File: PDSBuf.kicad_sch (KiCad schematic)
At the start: 23 parts

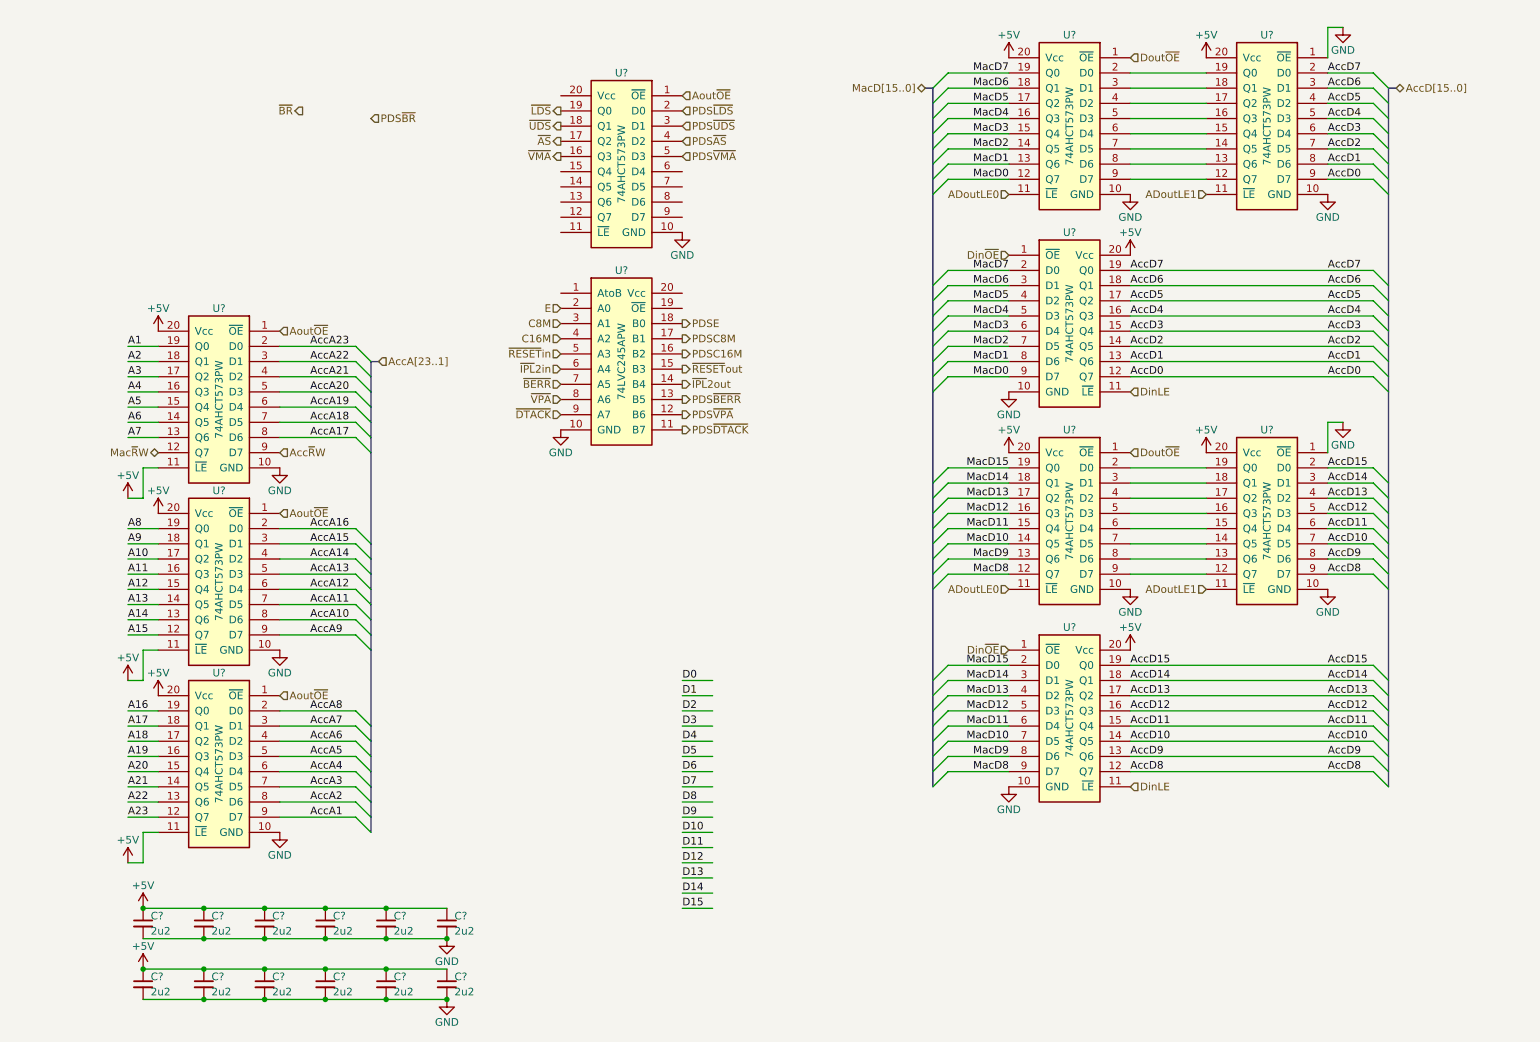
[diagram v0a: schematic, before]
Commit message: Switch to '030
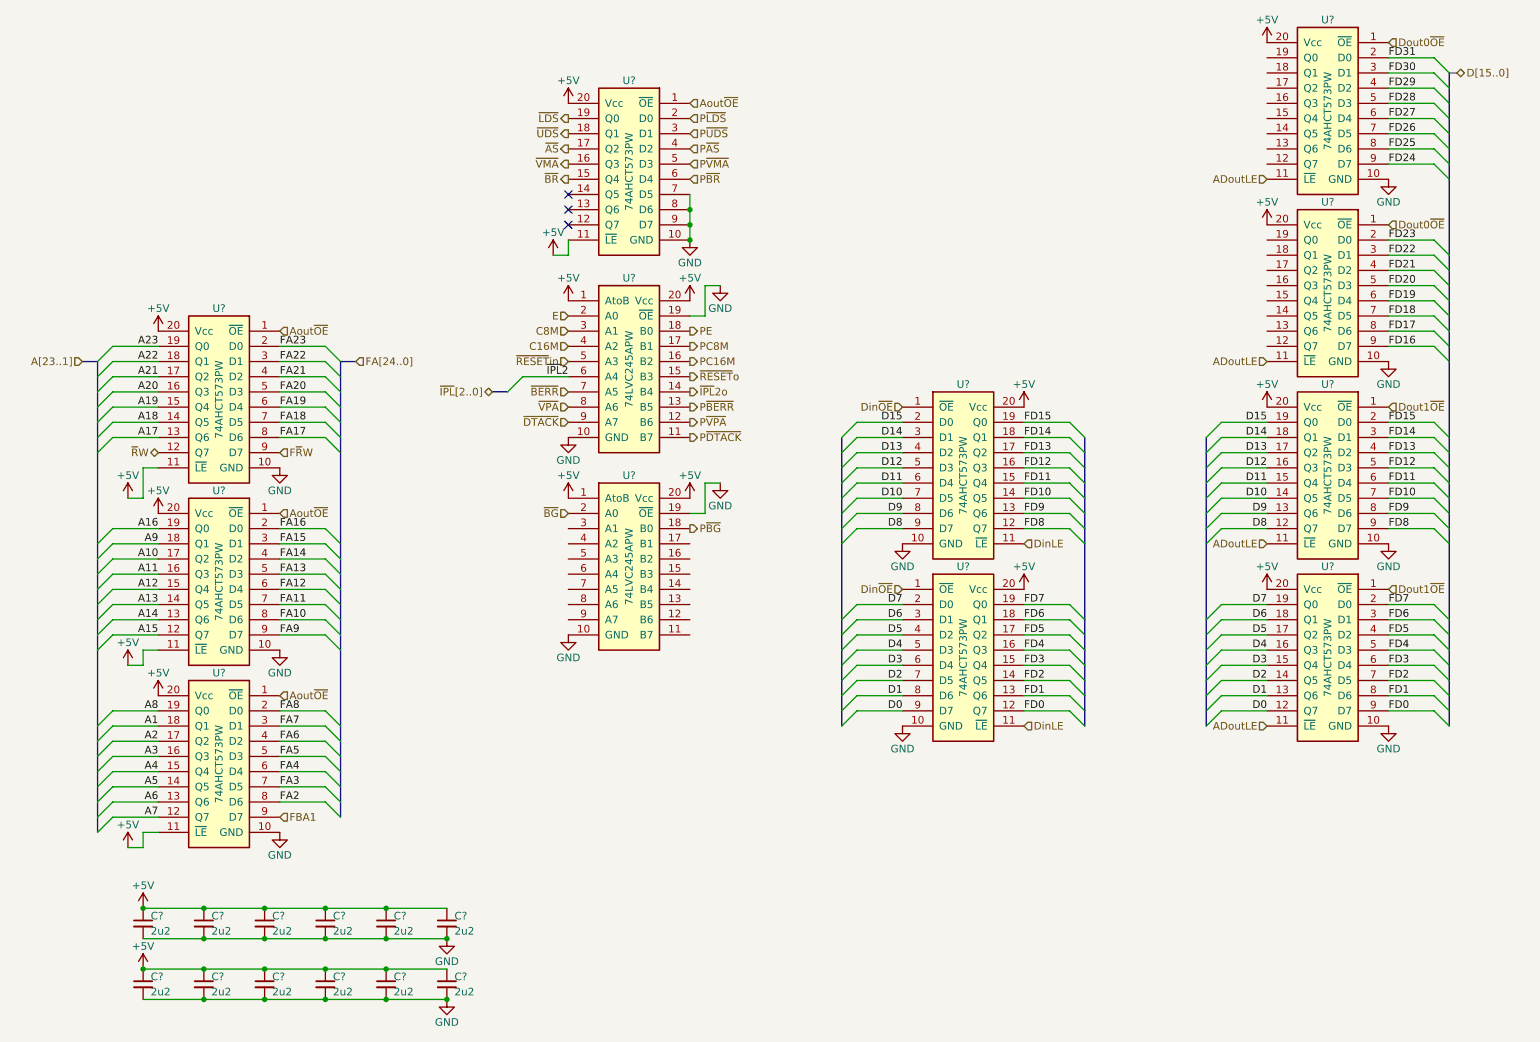
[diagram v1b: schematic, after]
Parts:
- removed U? (x5): 74AHCT573PW, stdpads:TSSOP-20_4.4x6.5mm_P0.65mm, symbol GW_Logic:74573
- added U? (x5): 74AHCT573PW, stdpads:TSSOP-20_4.4x6.5mm_P0.65mm, symbol GW_Logic:74573
- added U?: 74LVC245APW, symbol GW_Logic:74245
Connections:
- net +5V: now also U?.1 (AtoB), U?.11 (~{LE}), U?.20 (Vcc), U?.20 (Vcc), U?.1 (AtoB), U?.20 (Vcc), U?.20 (Vcc), U?.20 (Vcc), U?.20 (Vcc), U?.20 (Vcc), U?.20 (Vcc)
- net A1: now also U?.18 (Q1); no longer U?.19 (Q0)
- net A16: now also U?.19 (Q0); no longer U?.19 (Q0)
- net A17: now also U?.13 (Q6); no longer U?.18 (Q1)
- net A18: now also U?.14 (Q5); no longer U?.17 (Q2)
- net A19: now also U?.15 (Q4); no longer U?.16 (Q3)
- net A2: now also U?.17 (Q2); no longer U?.18 (Q1)
- net A20: now also U?.16 (Q3); no longer U?.15 (Q4)
- net A21: now also U?.17 (Q2); no longer U?.14 (Q5)
- net A22: now also U?.18 (Q1); no longer U?.13 (Q6)
- net A23: now also U?.19 (Q0); no longer U?.12 (Q7)
- net A3: now also U?.16 (Q3); no longer U?.17 (Q2)
- net A4: now also U?.15 (Q4); no longer U?.16 (Q3)
- net A5: now also U?.14 (Q5); no longer U?.15 (Q4)
- net A6: now also U?.13 (Q6); no longer U?.14 (Q5)
- net A7: now also U?.12 (Q7); no longer U?.13 (Q6)
- net A8: now also U?.19 (Q0); no longer U?.19 (Q0)
- net D0: now also U?.12 (Q7), U?.9 (D7)
- net D1: now also U?.13 (Q6), U?.8 (D6)
- net D10: now also U?.14 (Q5), U?.7 (D5)
- net D11: now also U?.15 (Q4), U?.6 (D4)
- net D12: now also U?.16 (Q3), U?.5 (D3)
- net D13: now also U?.17 (Q2), U?.4 (D2)
- net D14: now also U?.18 (Q1), U?.3 (D1)
- net D15: now also U?.19 (Q0), U?.2 (D0)
- net D2: now also U?.14 (Q5), U?.7 (D5)
- net D3: now also U?.15 (Q4), U?.6 (D4)
- net D4: now also U?.16 (Q3), U?.5 (D3)
- net D5: now also U?.17 (Q2), U?.4 (D2)
- net D6: now also U?.18 (Q1), U?.3 (D1)
- net D7: now also U?.19 (Q0), U?.2 (D0)
- net D8: now also U?.12 (Q7), U?.9 (D7)
- net D9: now also U?.13 (Q6), U?.8 (D6)
- net DinLE: now also U?.11 (~{LE}), U?.11 (~{LE})
- net Din~{OE}: now also U?.1 (~{OE}), U?.1 (~{OE})
- net GND: now also U?.19 (~{OE}), U?.7 (D5), U?.8 (D6), U?.9 (D7), U?.10 (GND), U?.10 (GND), U?.10 (GND), U?.10 (GND), U?.10 (GND), U?.10 (GND), U?.19 (~{OE}); no longer U?.1 (~{OE})
- net ~{BR}: now also U?.15 (Q4)
- net P~{BR}: now reaches U?.6 (D4)
- net ADoutLE1 renamed ADoutLE
- net ADoutLE: now also U?.11 (~{LE}), U?.11 (~{LE}), U?.11 (~{LE})
- net AccA1 renamed FBA1
- net AccA10 renamed FA10
- net AccA11 renamed FA11
- net AccA12 renamed FA12
- net AccA13 renamed FA13
- net AccA14 renamed FA14
- net AccA15 renamed FA15
- net AccA16 renamed FA16
- net AccA17 renamed FA17
- net AccA18 renamed FA18
- net AccA19 renamed FA19
- net AccA2 renamed FA2
- net AccA20 renamed FA20
- net AccA21 renamed FA21
- net AccA22 renamed FA22
- net AccA23 renamed FA23
- net AccA3 renamed FA3
- net AccA4 renamed FA4
- net AccA5 renamed FA5
- net AccA6 renamed FA6
- net AccA7 renamed FA7
- net AccA8 renamed FA8
- net AccA9 renamed FA9
- net AccD10 renamed FD10
- net FD10: now also U?.14 (Q5)
- net AccD11 renamed FD11
- net FD11: now also U?.15 (Q4)
- net AccD12 renamed FD12
- net FD12: now also U?.16 (Q3)
- net AccD13 renamed FD13
- net FD13: now also U?.17 (Q2)
- net AccD14 renamed FD14
- net FD14: now also U?.18 (Q1)
- net AccD15 renamed FD15
- net FD15: now also U?.19 (Q0)
- net AccD8 renamed FD8
- net FD8: now also U?.12 (Q7)
- net AccD9 renamed FD9
- net FD9: now also U?.13 (Q6)
- net Acc~{R}W renamed F~{R}W
- net Mac~{R}W renamed ~{R}W
- net PDSC16M renamed PC16M
- net PDSC8M renamed PC8M
- net PDSE renamed PE
- net PDS~{AS} renamed P~{AS}
- net PDS~{BERR} renamed P~{BERR}
- net PDS~{DTACK} renamed P~{DTACK}
- net PDS~{LDS} renamed P~{LDS}
- net PDS~{UDS} renamed P~{UDS}
- net PDS~{VMA} renamed P~{VMA}
- net PDS~{VPA} renamed P~{VPA}
- net ~{IPL}2in renamed ~{IPL}2
- net ~{IPL}2out renamed ~{IPL}2o
- net ~{RESET}out renamed ~{RESET}o
- new net Dout0~{OE}: U?.1 (~{OE}), U?.1 (~{OE})
- new net Dout1~{OE}: U?.1 (~{OE}), U?.1 (~{OE})
- new net FD0: U?.12 (Q7), U?.9 (D7)
- new net FD1: U?.13 (Q6), U?.8 (D6)
- new net FD16: U?.9 (D7)
- new net FD17: U?.8 (D6)
- new net FD18: U?.7 (D5)
- new net FD19: U?.6 (D4)
- new net FD2: U?.14 (Q5), U?.7 (D5)
- new net FD20: U?.5 (D3)
- new net FD21: U?.4 (D2)
- new net FD22: U?.3 (D1)
- new net FD23: U?.2 (D0)
- new net FD24: U?.9 (D7)
- new net FD25: U?.8 (D6)
- new net FD26: U?.7 (D5)
- new net FD27: U?.6 (D4)
- new net FD28: U?.5 (D3)
- new net FD29: U?.4 (D2)
- new net FD3: U?.15 (Q4), U?.6 (D4)
- new net FD30: U?.3 (D1)
- new net FD31: U?.2 (D0)
- new net FD4: U?.16 (Q3), U?.5 (D3)
- new net FD5: U?.17 (Q2), U?.4 (D2)
- new net FD6: U?.18 (Q1), U?.3 (D1)
- new net FD7: U?.19 (Q0), U?.2 (D0)
- new net P~{BG}: U?.18 (B0)
- new net ~{BG}: U?.2 (A0)
- no-connect marks 0 -> 3
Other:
- moved on the sheet: U?

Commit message: more
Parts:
- removed U? (x7): 74AHCT573PW, stdpads:TSSOP-20_4.4x6.5mm_P0.65mm, symbol GW_Logic:74573
- removed U? (x2): 74LVC245APW, symbol GW_Logic:74245
- added R? (x3): 47, symbol Device:R_Small
- added U? (x2): 74LVC245APW, symbol GW_Logic:74245
- added U? (x3): 74AHC245PW, symbol GW_Logic:74245
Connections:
- net F~{R}W is gone; now on net FA16: U?.9 (D7)
- net +5V: no longer U?.11 (~{LE}), U?.11 (~{LE}), U?.11 (~{LE})
- net A1: now also U?.12 (Q7); no longer U?.18 (Q1)
- net A10: now also U?.14 (Q5); no longer U?.17 (Q2)
- net A11: now also U?.15 (Q4); no longer U?.16 (Q3)
- net A12: now also U?.16 (Q3); no longer U?.15 (Q4)
- net A13: now also U?.17 (Q2); no longer U?.14 (Q5)
- net A14: now also U?.18 (Q1); no longer U?.13 (Q6)
- net A15: now also U?.19 (Q0); no longer U?.12 (Q7)
- net A16: now also U?.12 (Q7); no longer U?.19 (Q0)
- net A2: now also U?.13 (Q6); no longer U?.17 (Q2)
- net A3: now also U?.14 (Q5); no longer U?.16 (Q3)
- net A5: now also U?.16 (Q3); no longer U?.14 (Q5)
- net A6: now also U?.17 (Q2); no longer U?.13 (Q6)
- net A7: now also U?.18 (Q1); no longer U?.12 (Q7)
- net A8: now also U?.12 (Q7); no longer U?.19 (Q0)
- net A9: now also U?.13 (Q6); no longer U?.18 (Q1)
- net Aout~{OE}: now also U?.19 (~{OE})
- net C16M: now also U?.18 (B0)
- net C8M: now also U?.16 (B2)
- net D0: now also U?.11 (B7)
- net D1: now also U?.12 (B6)
- net D10: now also U?.13 (B5)
- net D11: now also U?.14 (B4)
- net D12: now also U?.15 (B3)
- net D13: now also U?.16 (B2)
- net D14: now also U?.17 (B1)
- net D15: now also U?.18 (B0)
- net D2: now also U?.13 (B5)
- net D3: now also U?.14 (B4)
- net D4: now also U?.15 (B3)
- net D5: now also U?.16 (B2)
- net D6: now also U?.17 (B1)
- net D7: now also U?.18 (B0)
- net D8: now also U?.11 (B7)
- net D9: now also U?.12 (B6)
- net E: now also U?.14 (B4)
- net FA10: now also U?.7 (D5); no longer U?.8 (D6)
- net FA11: now also U?.6 (D4); no longer U?.7 (D5)
- net FA12: now also U?.5 (D3); no longer U?.6 (D4)
- net FA13: now also U?.4 (D2); no longer U?.5 (D3)
- net FA14: now also U?.3 (D1); no longer U?.4 (D2)
- net FA15: now also U?.2 (D0); no longer U?.3 (D1)
- net FA16: no longer U?.2 (D0)
- net FA8: now also U?.9 (D7); no longer U?.2 (D0)
- net FA9: now also U?.8 (D6); no longer U?.9 (D7)
- net FD0: now also U?.9 (A7)
- net FD1: now also U?.8 (A6)
- net FD10: now also U?.7 (A5)
- net FD11: now also U?.6 (A4)
- net FD12: now also U?.5 (A3)
- net FD13: now also U?.4 (A2)
- net FD14: now also U?.3 (A1)
- net FD15: now also U?.2 (A0)
- net FD2: now also U?.7 (A5)
- net FD3: now also U?.6 (A4)
- net FD4: now also U?.5 (A3)
- net FD5: now also U?.4 (A2)
- net FD6: now also U?.3 (A1)
- net FD7: now also U?.2 (A0)
- net FD8: now also U?.9 (A7)
- net FD9: now also U?.8 (A6)
- net GND: now also U?.1 (AtoB), U?.1 (AtoB), U?.10 (GND), U?.10 (GND), U?.10 (GND), U?.10 (GND), U?.10 (GND), U?.11 (B7), U?.12 (B6), U?.14 (B4), U?.17 (B1), U?.19 (~{OE}), U?.3 (A1), U?.6 (A4), U?.8 (A6)
- net ~{AS}: now also U?.13 (B5)
- net ~{BERR}: now also U?.13 (B5)
- net ~{BG}: now also U?.18 (B0)
- net ~{BR}: now also U?.3 (A1)
- net ~{DTACK}: now also U?.15 (B3)
- net ~{IPL}2: now also U?.13 (B5)
- net ~{LDS}: now also U?.16 (B2)
- net ~{R}W: now also U?.18 (B0); no longer U?.12 (Q7)
- net ~{UDS}: now also U?.15 (B3)
- net ~{VMA}: now also U?.11 (B7)
- net ~{VPA}: now also U?.16 (B2)
- net FBA1 renamed FA1
- new net: R?.1, U?.4 (A2)
- new net: R?.1, U?.2 (A0)
- new net: R?.1, U?.6 (A4)
- new net +3V3: U?.1 (AtoB), U?.20 (Vcc), U?.20 (Vcc), U?.20 (Vcc), U?.20 (Vcc)
- new net AHoutLE: U?.11 (~{LE}), U?.11 (~{LE})
- new net ALoutLE: U?.11 (~{LE})
- new net BC16M: R?.2
- new net BC8M: R?.2
- new net BE: R?.2
- new net B~{BERR}: U?.7 (A5)
- new net B~{BG}: U?.2 (A0)
- new net B~{DTACK}: U?.5 (A3)
- new net B~{IPL}0: U?.9 (A7)
- new net B~{IPL}1: U?.8 (A6)
- new net B~{IPL}2: U?.7 (A5)
- new net B~{RESET}: U?.6 (A4)
- new net B~{VPA}: U?.4 (A2)
- new net DDIR: U?.1 (AtoB), U?.1 (AtoB)
- new net D~{OE}: U?.19 (~{OE}), U?.19 (~{OE})
- new net O~{AS}: U?.7 (A5)
- new net O~{BR}: U?.17 (B1)
- new net O~{LDS}: U?.4 (A2)
- new net O~{R}W: U?.2 (A0)
- new net O~{UDS}: U?.5 (A3)
- new net O~{VMA}: U?.9 (A7)
- new net ~{IPL}0: U?.11 (B7)
- new net ~{IPL}1: U?.12 (B6)
- new net ~{RESET}: U?.14 (B4)
- no-connect marks 3 -> 0

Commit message: more
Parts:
- removed R?: 47, symbol Device:R_Small
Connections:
- net +3V3: now also U?.20 (Vcc)
- net A8: now also U?.19 (Q0); no longer U?.12 (Q7)
- net BE: now also U?.6 (A4)
- net B~{BERR}: now also U?.8 (A6); no longer U?.7 (A5)
- net FA8: now also U?.2 (D0); no longer U?.9 (D7)
- net GND: now also U?.12 (Q7), U?.13 (B5), U?.15 (B3), U?.17 (B1), U?.19 (~{OE}), U?.3 (A1), U?.5 (A3), U?.7 (A5), U?.9 (A7), U?.9 (D7)
- net ~{BERR}: now also U?.12 (B6); no longer U?.13 (B5)
- net AHoutLE renamed AHLE
- net ALoutLE renamed ALLE
- net Aout~{OE} renamed A~{OE}
- net FD0 renamed BD0
- net FD1 renamed BD1
- net FD10 renamed BD10
- net FD11 renamed BD11
- net FD12 renamed BD12
- net FD13 renamed BD13
- net FD14 renamed BD14
- net FD15 renamed BD15
- net FD2 renamed BD2
- net FD3 renamed BD3
- net FD4 renamed BD4
- net FD5 renamed BD5
- net FD6 renamed BD6
- net FD7 renamed BD7
- net FD8 renamed BD8
- net FD9 renamed BD9
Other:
- moved on the sheet: R?

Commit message: idk
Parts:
- removed C? (x11): 2u2, stdpads:C_0603, symbol Device:C_Small
- removed R? (x2): 47, symbol Device:R_Small
- removed U? (x3): 74AHC245PW, symbol GW_Logic:74245
- added C2, C33, C34, C35, C36, C37, C38, C39, C5, C6: 1u, stdpads:C_0402, symbol Device:C_Small
- added R1, R12, R2, R3, R4, R6: 47, symbol Device:R_Small
- added U1, U2: 74LVC1G04GW, stdpads:SOT-353, symbol GW_Logic:741G04GW
- added U10: 74LVC245APW, symbol GW_Logic:74245
- added U4: 74AHCT573PW, stdpads:TSSOP-20_4.4x6.5mm_P0.65mm, symbol GW_Logic:74573
- added U5, U8: 74AHCT1G125GW, stdpads:SOT-353, symbol GW_Logic:741G125GW
- C1: renamed from C?; value 2u2 -> 1u; footprint stdpads:C_0603 -> stdpads:C_0402; LCSC Part C23630 -> C52923
- gave numbers to parts that had none: 5
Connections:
- net ALLE is gone; now on net ALE: U15.11 (~{LE})
- net +3V3: now also U1.5 (Vcc), U10.20 (Vcc), U2.5 (Vcc), U5.5 (Vcc), U8.5 (Vcc)
- net +5V: now also C2.1, C33.1, C34.1, C35.1, C36.1, C37.1, C38.1, C39.1, C5.1, C6.1, U4.11 (~{LE}), U4.20 (Vcc)
- net A~{OE}: now also U4.1 (~{OE})
- net BE: now also U10.2 (A0)
- net B~{BERR}: now also U10.3 (A1)
- net B~{DTACK}: now also U10.5 (A3)
- net B~{IPL}0: now also R6.2
- net B~{IPL}1: now also R4.2
- net B~{IPL}2: now also R3.2
- net B~{RESET}: now also R12.2
- net B~{VPA}: now also U10.4 (A2)
- net C16M: now also U1.2 (A)
- net C8M: now also U2.2 (A)
- net E: now also U10.18 (B0)
- net GND: now also C2.2, C33.2, C34.2, C35.2, C36.2, C37.2, C38.2, C39.2, C5.2, C6.2, U1.3 (GND), U10.1 (AtoB), U10.10 (GND), U10.19 (~{OE}), U2.3 (GND), U4.10 (GND), U4.13 (Q6), U4.15 (Q4), U4.18 (Q1), U4.3 (D1), U4.6 (D4), U4.8 (D6), U5.1 (~{OE}), U5.3 (GND), U8.2 (A), U8.3 (GND)
- net O~{AS}: now also U4.7 (D5)
- net O~{BR}: now also U5.2 (A)
- net O~{LDS}: now also U4.4 (D2)
- net O~{R}W: now also U4.2 (D0)
- net O~{UDS}: now also U4.5 (D3)
- net O~{VMA}: now also U4.9 (D7)
- net ~{AS}: now also U4.14 (Q5)
- net ~{BERR}: now also U10.17 (B1)
- net ~{BR}: now also U5.4 (Y)
- net ~{DTACK}: now also U10.15 (B3)
- net ~{IPL}0: now also U10.11 (B7)
- net ~{IPL}1: now also U10.12 (B6)
- net ~{IPL}2: now also U10.13 (B5)
- net ~{LDS}: now also U4.17 (Q2)
- net ~{RESET}: now also U10.14 (B4), U8.4 (Y)
- net ~{R}W: now also U4.19 (Q0)
- net ~{UDS}: now also U4.16 (Q3)
- net ~{VMA}: now also U4.12 (Q7)
- net ~{VPA}: now also U10.16 (B2)
- net AHLE renamed ALE
- new net: R3.1, U10.7 (A5)
- new net: R1.1, U1.4 (Y)
- new net: R2.1, U2.4 (Y)
- new net: R6.1, U10.9 (A7)
- new net: R12.1, U10.6 (A4)
- new net: R4.1, U10.8 (A6)
- new net B~{C16M}: R2.2
- new net B~{C8M}: R1.2
- new net O~{RESET}: U8.1 (~{OE})
- no-connect marks 0 -> 2
